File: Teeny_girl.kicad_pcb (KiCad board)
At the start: 4 copper layers, 110 x 105 mm, 67 parts, among them J1 Conn_01x40, J2 USB_B_Micro, J3 40HAT, J4 Conn_01x03, J5 Conn_01x04, J6 USB_C_Receptacle, SW1 SW_Push, SW10 SW_Push, SW11 SW_Push, SW12 SW_Push, SW16 SW_Push_Open, SW2 SW_Push, SW3 SW_Push, SW4 SW_Push, SW5 SW_Push, SW6 SW_Push, SW7 SW_Push, SW8 SW_Push, SW9 SW_Push, U1 AMS1117-3.3, U2 MCP73831-2-OT, U3 Display-position, U5 TPS61161_, U6 STM32F103C6T6, Y1 32.768k, Y2 8M

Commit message: saved
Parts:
- removed C7: 1uF, Capacitor_SMD:C_0805_2012Metric
- removed J1: Conn_01x40, YZ-Connector:TE_4-1734839-0_1x40-1MP_P0.5mm_Horizontal
- removed J2: USB_B_Micro, Connector_USB:USB_Micro-AB_Molex_47590-0001
- removed R8, R9: 10K, Resistor_SMD:R_0603_1608Metric
- added C17: 1uF, Capacitor_SMD:C_0805_2012Metric, B.Cu at (155.2, 69.3)
- added D1: ESD56151W04, Diode_SMD:D_SOD-323, B.Cu at (174.4, 27.5)
- added H1: MountingHole, MountingHole:MountingHole_3.2mm_M3_DIN965_Pad, F.Cu at (81.5, 47.1)
- added H2: MountingHole, MountingHole:MountingHole_3.2mm_M3_DIN965_Pad, F.Cu at (204.0, 47.1)
- added H3: MountingHole, MountingHole:MountingHole_3.2mm_M3_DIN965_Pad, F.Cu at (81.5, 96.1)
- added H4: MountingHole, MountingHole:MountingHole_3.2mm_M3_DIN965_Pad, F.Cu at (204.0, 96.1)
- added J7: 54FPC, YZ-Connector:AMPHENOL_54fpc, B.Cu at (134.5, 50.7)
- added R17: 10K, Resistor_SMD:R_0603_1608Metric, B.Cu at (150.5, 67.5)
- added R4: 10K, Resistor_SMD:R_0603_1608Metric, B.Cu at (150.6, 69.4)
- C10, C11, C12, C13, C14, C20, C21, C22, C23, C8, C9, D4, D5, J4, R10, R14, R15, R16, SW16, U6, Y1, Y2: moved to B.Cu
- J3: footprint YZ-Connector:PinHeader_2x20_P2.54mm_Vertical_PTH -> YZ-Connector:PinHeader_2x20_P2.54mm_Vertical_SMD
- U3: footprint YZ-LOGO:Display-position -> YZ-LOGO:Display-position_3.5
- moved SW5 124.6 mm to (94.8, 43.6)
- moved SW10 112.7 mm to (196.6, 43.3)
- moved SW16 106.0 mm to (179.9, 42.2)
- moved R10 100.8 mm to (184.0, 47.7)
- moved R3 97.3 mm to (106.6, 90.3), turned to -90 degrees
- moved C12 96.2 mm to (184.0, 49.5)
- moved J5 95.2 mm to (209.4, 54.7), turned to 180 degrees
- moved R2 93.3 mm to (110.0, 90.3), turned to -90 degrees
- moved C14 93.0 mm to (175.8, 49.4), turned to 90 degrees
- moved D4 87.9 mm to (103.3, 43.6), turned to 0 degrees
- moved D5 87.9 mm to (103.3, 46.1), turned to 0 degrees
- moved R15 87.6 mm to (186.4, 51.9), turned to 180 degrees
- moved R16 87.6 mm to (186.4, 53.9), turned to 180 degrees
- moved R1 86.3 mm to (113.0, 90.2), turned to -90 degrees
- moved J4 84.5 mm to (164.5, 46.0), turned to 180 degrees
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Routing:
- removed copper zone on B.Cu, net GND
- removed copper zone on F.Cu, net GND
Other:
- board size 110 x 105 mm -> 137.5 x 64 mm
- copper layers 4 -> 2

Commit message: save 2/20
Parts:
- removed BT1: Battery_Cell, Connector_PinHeader_2.54mm:PinHeader_1x02_P2.54mm_Vertical
- removed D1: ESD56151W04, Diode_SMD:D_SOD-323
- removed J6: USB_C_Receptacle, YZ-Connector:USB_C_Receptacle_Amphenol_12401610E4-2A
- removed JP2: SolderJumper_3_Open, Jumper:SolderJumper-3_P1.3mm_Open_Pad1.0x1.5mm
- added C15: 100nF, Capacitor_SMD:C_0603_1608Metric, B.Cu at (161.4, 62.0)
- added C16: 10u, Capacitor_SMD:C_0805_2012Metric_Pad1.18x1.45mm_HandSolder, B.Cu at (99.0, 46.3)
- added C18: 100nF, Capacitor_SMD:C_0603_1608Metric, B.Cu at (167.4, 62.0)
- added C19: 47UF, Capacitor_Tantalum_SMD:CP_EIA-3216-18_Kemet-A_Pad1.58x1.35mm_HandSolder, B.Cu at (167.4, 58.3)
- added C24: 47UF, Capacitor_Tantalum_SMD:CP_EIA-3216-18_Kemet-A_Pad1.58x1.35mm_HandSolder, B.Cu at (161.4, 58.3)
- added C25: 470uF, Capacitor_SMD:CP_Elec_6.3x7.7, B.Cu at (205.5, 83.2)
- added C26: 470uF, Capacitor_SMD:CP_Elec_6.3x7.7, B.Cu at (90.5, 97.3)
- added C27: 100nf, Capacitor_SMD:C_0603_1608Metric_Pad1.08x0.95mm_HandSolder, B.Cu at (202.2, 89.1)
- added C28: 100nf, Capacitor_SMD:C_0603_1608Metric_Pad1.08x0.95mm_HandSolder, B.Cu at (96.3, 99.3)
- added C29: 100UF, Capacitor_SMD:CP_Elec_6.3x5.4, B.Cu at (173.2, 44.8)
- added C30: 100UF, Capacitor_SMD:CP_Elec_6.3x5.4, B.Cu at (173.4, 62.8)
- added C31: 47UF, Capacitor_Tantalum_SMD:CP_EIA-3216-18_Kemet-A_Pad1.58x1.35mm_HandSolder, B.Cu at (176.2, 52.3)
- added C32: 10uF, Capacitor_SMD:C_0805_2012Metric, B.Cu at (155.3, 63.0)
- added C33: 10uF, Capacitor_SMD:C_0805_2012Metric, B.Cu at (155.4, 59.3)
- added C34: 22uF, Capacitor_SMD:C_0805_2012Metric, F.Cu at (158.7, 124.8)
- added C35: 22uF, Capacitor_SMD:C_0805_2012Metric, F.Cu at (158.7, 127.3)
- added C36: 22uF, Capacitor_SMD:C_0805_2012Metric, B.Cu at (130.2, 59.5)
- added C37: 22uF, Capacitor_SMD:C_0805_2012Metric, B.Cu at (132.4, 59.5)
- added C38: 22uF, Capacitor_SMD:C_0805_2012Metric, B.Cu at (134.7, 59.5)
- added C39: 22uF, Capacitor_SMD:C_0805_2012Metric, B.Cu at (136.9, 59.5)
- added C7: 10u, Capacitor_SMD:CP_Elec_4x5.4, B.Cu at (131.9, 91.5)
- added F1: 3A, Fuse:Fuse_1206_3216Metric, B.Cu at (29.0, 57.4)
- added G***: LOGO, LOGO, F.Cu at (82.1, 53.2)
- added G***: LOGO, LOGO, B.Cu at (82.1, 53.2)
- added G***: LOGO, LOGO, B.Cu at (187.2, 42.3)
- added G***: LOGO, LOGO, B.Cu at (132.4, 72.5)
- added G***: LOGO, LOGO, B.Cu at (144.4, 43.0)
- added G***: LOGO, LOGO, B.Cu at (102.7, 100.4)
- added G***: LOGO, LOGO, B.Cu at (98.4, 74.8)
- added G***: LOGO, LOGO, B.Cu at (210.0, 69.1)
- added J1: Battery, Connector_Molex:Molex_PicoBlade_53048-0310_1x03_P1.25mm_Horizontal, B.Cu at (49.4, 100.5)
- added J2: Conn_01x03, Jumper:SolderJumper-3_P1.3mm_Open_Pad1.0x1.5mm, B.Cu at (148.4, 65.3)
- added Je1: PJ-342B-TX-SMT, YZ-Connector:PJ-342B-TX-SMT_XKB, B.Cu at (157.5, 46.1)
- added L1: 1uH, YZ-PWR:IND_MGV05021R0M-10, B.Cu at (141.9, 62.0)
- added LED1: LED, LED_SMD:LED_0603_1608Metric, F.Cu at (163.4, 109.0)
- added LED2: LED, LED_SMD:LED_0603_1608Metric, F.Cu at (163.4, 112.0)
- added LED3: LED, LED_SMD:LED_0603_1608Metric, F.Cu at (163.6, 115.0)
- added LED4: LED, LED_SMD:LED_0603_1608Metric, F.Cu at (163.7, 118.0)
- added LS1: KAAG20008C-10A, YZ-Audio:CUI_CMS-15116-SP, F.Cu at (191.0, 92.1)
- added LS2: KAAG20008C-10A, YZ-Audio:CUI_CMS-15116-SP, F.Cu at (94.5, 92.1)
- added P1: USB_C_Plug_USB2.0, Connector_USB:USB_C_Receptacle_G-Switch_GT-USB-7010ASV, B.Cu at (105.5, 42.1)
- added Q1: BC846, Package_TO_SOT_SMD:SOT-23, B.Cu at (132.4, 64.8)
- added R18: 100, Resistor_SMD:R_0603_1608Metric_Pad0.98x0.95mm_HandSolder, B.Cu at (161.3, 64.0)
- added R19: 100, Resistor_SMD:R_0603_1608Metric_Pad0.98x0.95mm_HandSolder, B.Cu at (167.4, 63.9)
- added R20: 1K8, Resistor_SMD:R_0603_1608Metric_Pad0.98x0.95mm_HandSolder, B.Cu at (163.4, 57.3)
- added R21: 1K8, Resistor_SMD:R_0603_1608Metric_Pad0.98x0.95mm_HandSolder, B.Cu at (165.2, 57.3)
- added R22: 10K, Resistor_SMD:R_0603_1608Metric, B.Cu at (165.2, 50.0)
- added R23: 10K, Resistor_SMD:R_0603_1608Metric, B.Cu at (165.2, 53.5)
- added R24: 4.7, Resistor_SMD:R_0603_1608Metric, B.Cu at (96.3, 101.1)
- added R25: 4.7, Resistor_SMD:R_0603_1608Metric, B.Cu at (208.2, 89.1)
- added R26: 2, Resistor_SMD:R_0603_1608Metric, B.Cu at (155.2, 65.5)
- added R27: 0.5, Resistor_SMD:R_0603_1608Metric, F.Cu at (155.2, 124.8)
- added R28: 10K, Resistor_SMD:R_0603_1608Metric, B.Cu at (136.4, 63.8)
- added R29: 100K, Resistor_SMD:R_0603_1608Metric, B.Cu at (136.4, 65.8)
- added R30: 1k, Resistor_SMD:R_0603_1608Metric, F.Cu at (160.2, 109.0)
- added R31: 1k, Resistor_SMD:R_0603_1608Metric, F.Cu at (160.4, 112.0)
- added R32: 1k, Resistor_SMD:R_0603_1608Metric, F.Cu at (160.2, 115.0)
- added R33: 1k, Resistor_SMD:R_0603_1608Metric, F.Cu at (160.4, 118.0)
- added R8: 20, Resistor_SMD:R_0603_1608Metric, B.Cu at (105.7, 48.7)
- added R9: 20, Resistor_SMD:R_0603_1608Metric, B.Cu at (115.8, 44.3)
- added SW13: SW_Push, Button_Switch_THT:SW_Tactile_SPST_Angled_PTS645Vx39-2LFS, B.Cu at (206.3, 64.6)
- added U10: PESD5V0L5UV, Package_TO_SOT_SMD:SOT-363_SC-70-6_Handsoldering, B.Cu at (124.4, 44.5)
- added U11: PESD5V0L5UV, Package_TO_SOT_SMD:SOT-363_SC-70-6_Handsoldering, B.Cu at (201.0, 70.1)
- added U12: IP5306, YZ-ICs:IP5306 SOIC9P127_490X600X170L84X42T330X241N, B.Cu at (149.6, 60.9)
- added U4: XC6219B182MR, Package_TO_SOT_SMD:SOT-23-5, B.Cu at (192.4, 24.1)
- added U7: TDA2822D, YZ-Audio:SOIC127P600X175-8N, B.Cu at (170.2, 52.3)
- added U8: PESD5V0L5UV, Package_TO_SOT_SMD:SOT-363_SC-70-6_Handsoldering, F.Cu at (89.0, 71.5)
- added U9: PESD5V0L5UV, Package_TO_SOT_SMD:SOT-363_SC-70-6_Handsoldering, F.Cu at (196.3, 71.8)
- C17: footprint Capacitor_SMD:C_0805_2012Metric -> Capacitor_SMD:C_0603_1608Metric
- D4, D5, R15, R16: moved to F.Cu
- H1, H2, H3, H4: footprint MountingHole:MountingHole_3.2mm_M3_DIN965_Pad -> MountingHole:MountingHole_5mm
- J5: footprint Connector_PinHeader_2.54mm:PinHeader_1x04_P2.54mm_Vertical -> Connector_PinHeader_1.27mm:PinHeader_1x04_P1.27mm_Vertical
- R1, R2: value 20 -> 10k
- R11: value 20 -> 4K7
- R12: value 20 -> 5K1
- R13, R3: value 4K7 -> 220; footprint Resistor_SMD:R_0603_1608Metric -> Resistor_SMD:R_0603_1608Metric_Pad0.98x0.95mm_HandSolder
- R7: value 5 -> 10
- SW1, SW2, SW3, SW4, SW6, SW7, SW8, SW9: footprint YZ-Connector:SW_TL9210AF180Q -> Button_Switch_SMD:SW_SPST_TL3342
- SW10: footprint Button_Switch_THT:SW_Tactile_SPST_Angled_PTS645Vx83-2LFS -> Button_Switch_THT:SW_Tactile_SPST_Angled_PTS645Vx39-2LFS
- SW11, SW12: footprint YZ-Connector:SW_PUSH_6mm_H5mm -> Button_Switch_SMD:SW_SPST_TL3342
- SW5: value SW_Push -> locked; footprint Button_Switch_THT:SW_Tactile_SPST_Angled_PTS645Vx83-2LFS -> Button_Switch_THT:SW_Tactile_SPST_Angled_PTS645Vx39-2LFS
- U1: value AMS1117-3.3 -> NC7WZ16P6X; footprint Package_TO_SOT_SMD:SOT-223-3_TabPin2 -> YZ-ICs:SOT65P210X110-6N
- Y2: footprint Crystal:Crystal_SMD_5032-2Pin_5.0x3.2mm -> Crystal:Crystal_SMD_Abracon_ABM8AIG-4Pin_3.2x2.5mm
- moved JP1 168.7 mm to (96.9, 51.8)
- moved R11 144.5 mm to (117.7, 44.3)
- moved R12 141.5 mm to (120.2, 44.3)
- moved R15 114.3 mm to (77.4, 86.3), turned to 0 degrees
- moved R16 114.3 mm to (77.4, 88.3)
- moved R2 108.7 mm to (196.4, 24.3)
- moved SW12 103.0 mm to (193.5, 53.3)
- moved C4 99.5 mm to (201.3, 25.3)
- moved C2 98.9 mm to (188.9, 24.1)
- moved R13 93.8 mm to (167.4, 65.8), turned to 0 degrees
- moved R1 89.6 mm to (193.4, 50.7), turned to 0 degrees
- moved R3 59.9 mm to (161.4, 66.0), turned to 180 degrees
- moved U1 54.5 mm to (164.4, 64.3), turned to -90 degrees
- moved D2 52.1 mm to (42.0, 59.3), turned to 90 degrees
- moved R4 51.5 mm to (103.0, 49.7), turned to -90 degrees
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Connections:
- C1 pad 1: 3V7 -> 5V0_SW
- J7 pad 41: unconnected-(J7-IOVCC-Pad41) -> 3V3
- J7 pad 42: unconnected-(J7-VCI-Pad42) -> 3V3
- L2 pad 1: 3V7 -> 5V0_SW
- R1 pad 1: Net-(J6-D--PadA7) -> /Backlight_CTRL
- R1 pad 2: /PA11 -> GND
- R11 pad 1: Net-(J2-D+) -> /PA11
- R11 pad 2: /PA12 -> Net-(JP1-C)
- R12 pad 2: /PA11 -> 5V_USB
- R13 pad 1: /PA12 -> Net-(U1-Y2)
- R13 pad 2: Net-(JP1-C) -> Net-(C18-Pad1)
- R2 pad 1: Net-(J6-D+-PadA6) -> /ON_OFF_EN
- R2 pad 2: /PA12 -> GND
- R3 pad 1: /PA11 -> Net-(U1-Y1)
- U1 pad 1: GND -> /PWM_0
- U1 pad 2: 3V3 -> unconnected-(U1-GND-Pad2)
- U1 pad 3: 3V7 -> /PWM_1
- U5 pad 6: 3V7 -> 5V0_SW
- U6 pad 18: unconnected-(U6-PB0-Pad18) -> /ON_OFF
- U6 pad 19: unconnected-(U6-PB1-Pad19) -> /ON_OFF_EN
- U6 pad 20: unconnected-(U6-PB2-Pad20) -> /PWR_EN
- U6 pad 31: unconnected-(U6-PA10-Pad31) -> /Backlight_CTRL
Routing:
- net /B2: track 0.00 -> 131.9 mm, vias 0 -> 2
- net /HSYNC: track 0.00 -> 120.8 mm
- net /B5: track 0.00 -> 119.5 mm, vias 0 -> 2
- net /VSYNC: track 0.00 -> 114.2 mm
- net /B6: track 0.00 -> 112.6 mm, vias 0 -> 4
- net /B7: track 0.00 -> 109.9 mm, vias 0 -> 2
- net /G6: track 0.00 -> 108.8 mm, vias 0 -> 2
- net /G7: track 0.00 -> 106.2 mm, vias 0 -> 4
- net /B3: track 0.00 -> 101.7 mm, vias 0 -> 2
- net /LED_A: track 0.00 -> 101.6 mm
- net /R3: track 0.00 -> 101.1 mm, vias 0 -> 2
- net /G2: track 0.00 -> 100.7 mm, vias 0 -> 2
- net /LED_K: track 0.00 -> 99.6 mm
- net /R4: track 0.00 -> 96.8 mm, vias 0 -> 2
- net /B4: track 0.00 -> 96.8 mm, vias 0 -> 2
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- added copper zone on B.Cu, net 5V0_SW
- added copper zone on B.Cu, net GND
- added copper zone on F.Cu, net GND
- added copper zone on B.Cu, net Net-(D3-A)
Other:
- outline, holes or cut-outs redrawn

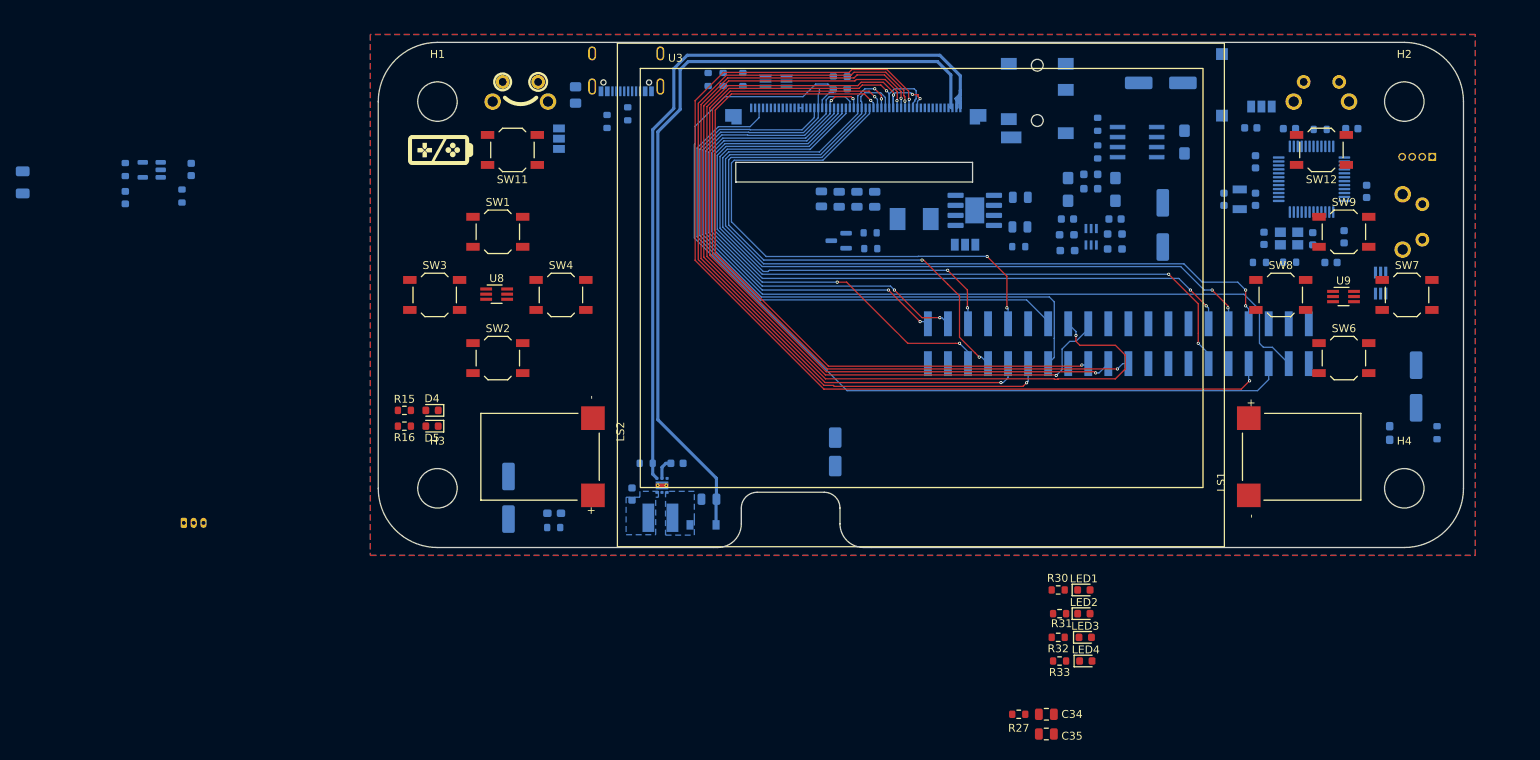
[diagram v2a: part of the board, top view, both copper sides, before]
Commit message: updated and delete old battery charger mcp73871
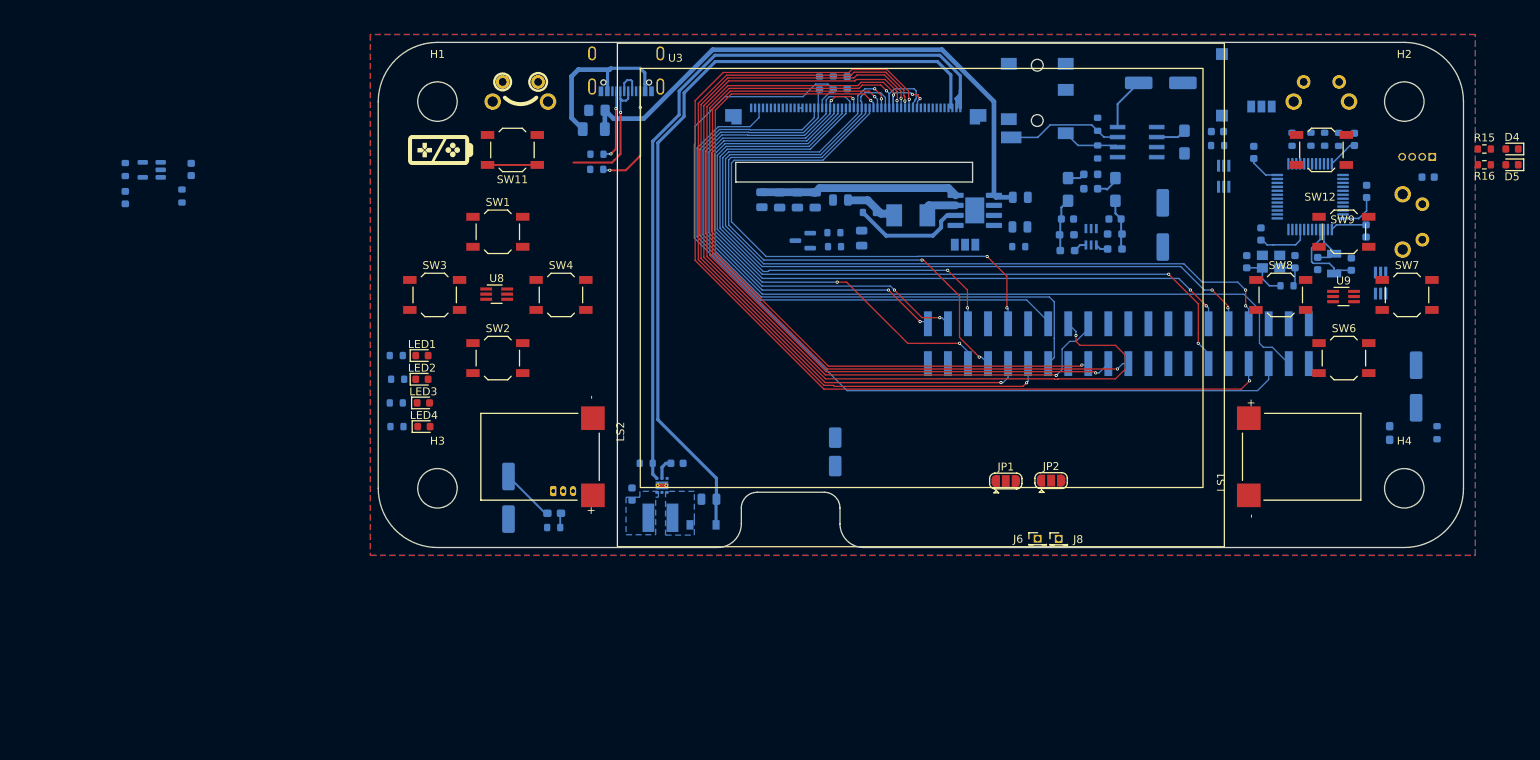
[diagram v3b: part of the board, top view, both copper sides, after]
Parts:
- removed F1: 3A, Fuse:Fuse_1206_3216Metric
- added F2: 3A, Fuse:Fuse_1206_3216Metric, B.Cu at (101.4, 50.6)
- added J6: DM, Connector_PinHeader_1.27mm:PinHeader_1x01_P1.27mm_Vertical, F.Cu at (157.6, 102.5)
- added J8: DP, Connector_PinHeader_1.27mm:PinHeader_1x01_P1.27mm_Vertical, F.Cu at (160.3, 102.5)
- added JP2: SolderJumper_3_Open, Jumper:SolderJumper-3_P1.3mm_Open_RoundedPad1.0x1.5mm, F.Cu at (159.3, 95.2)
- added R34: 5K1, Resistor_SMD:R_0603_1608Metric, B.Cu at (101.7, 55.7)
- C34, C35, R27, R30, R31, R32, R33: moved to B.Cu
- JP1: footprint Jumper:SolderJumper-3_P1.3mm_Open_Pad1.0x1.5mm -> Jumper:SolderJumper-3_P1.3mm_Open_RoundedPad1.0x1.5mm; moved to F.Cu
- R11: value 4K7 -> 1k5
- moved D4 140.8 mm to (217.7, 53.2)
- moved D5 140.8 mm to (217.7, 55.2)
- moved R15 140.8 mm to (214.2, 53.2)
- moved R16 140.8 mm to (214.2, 55.2)
- moved R33 89.1 mm to (76.4, 88.3)
- moved LED3 89.0 mm to (79.8, 85.3)
- moved R31 89.0 mm to (76.5, 82.3)
- moved LED1 89.0 mm to (79.6, 79.3)
- moved LED2 89.0 mm to (79.6, 82.3)
- moved LED4 89.0 mm to (79.8, 88.3)
- moved R30 89.0 mm to (76.3, 79.3)
- moved R32 89.0 mm to (76.3, 85.3)
- moved R8 86.6 mm to (192.2, 51.9)
- moved R9 80.2 mm to (195.7, 51.9)
- moved R11 76.6 mm to (194.0, 51.9), turned to 90 degrees
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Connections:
- J1 pad 2: Net-(J1-Pin_2) -> 3V7
- JP1 pad 1: 5V_USB -> Net-(J6-Pin_1)
- JP1 pad 3: 3V3 -> Net-(JP1-B)
- P1 pad A4: 5V_USB -> Net-(F2-Pad1)
- P1 pad A6: Net-(P1-D+) -> Net-(JP2-B)
- P1 pad A7: Net-(P1-D-) -> Net-(JP1-B)
- P1 pad A8: (no net) -> unconnected-(P1-SBU1-PadA8)
- P1 pad A9: 5V_USB -> Net-(F2-Pad1)
- P1 pad B4: 5V_USB -> Net-(F2-Pad1)
- P1 pad B5: unconnected-(P1-VCONN-PadB5) -> Net-(P1-CC2)
- P1 pad B6: (no net) -> Net-(JP2-B)
- P1 pad B7: (no net) -> Net-(JP1-B)
- P1 pad B8: (no net) -> unconnected-(P1-SBU2-PadB8)
- P1 pad B9: 5V_USB -> Net-(F2-Pad1)
- R11 pad 1: /PA11 -> /PA12
- R11 pad 2: Net-(JP1-C) -> 3V3
- R12 pad 2: 5V_USB -> GND
- R8 pad 1: Net-(P1-D-) -> Net-(JP1-C)
- R9 pad 1: Net-(P1-D+) -> Net-(JP2-C)
- U6 pad 21: unconnected-(U6-PB10-Pad21) -> /KEY_B
- U6 pad 22: unconnected-(U6-PB11-Pad22) -> /KEY_C
- U6 pad 25: unconnected-(U6-PB12-Pad25) -> /KEY_D
- U6 pad 26: unconnected-(U6-PB13-Pad26) -> /RIGHT_TRIGGER
- U6 pad 27: unconnected-(U6-PB14-Pad27) -> /START
- U6 pad 28: unconnected-(U6-PB15-Pad28) -> /SELECT
- U6 pad 40: unconnected-(U6-PB4-Pad40) -> /KEY_UP
- U6 pad 41: unconnected-(U6-PB5-Pad41) -> /KEY_DOWN
- U6 pad 42: unconnected-(U6-PB6-Pad42) -> /KEY_LEFT
- U6 pad 43: unconnected-(U6-PB7-Pad43) -> /KEY_RIGHT
- U6 pad 45: unconnected-(U6-PB8-Pad45) -> /LEFT_TRIGGER
- U6 pad 46: unconnected-(U6-PB9-Pad46) -> /KEY_A
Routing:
- net 5V_USB: track 0.00 -> 72.8 mm
- net 5V0_SW: track 0.00 -> 29.0 mm
- net 3V3: track 0.50 -> 25.0 mm
- net Net-(F2-Pad1): track 0.00 -> 22.7 mm
- net Net-(JP1-B): track 0.00 -> 16.5 mm, vias 0 -> 1
- net /AUDIO_L: track 0.00 -> 14.8 mm
- net Net-(U12-BAT): track 0.00 -> 14.5 mm
- net Net-(P1-CC2): track 0.00 -> 13.7 mm, vias 0 -> 2
- net /PC15: track 0.00 -> 10.7 mm
- net Net-(P1-CC1): track 0.00 -> 9.18 mm, vias 0 -> 2
- net /AUDIO_R: track 0.00 -> 7.30 mm
- net Net-(C26-Pad2): track 0.00 -> 6.86 mm
- net Net-(C15-Pad2): track 0.00 -> 6.72 mm
- net Net-(C29-Pad1): track 0.00 -> 6.70 mm
- net 3V7: track 0.00 -> 6.51 mm
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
